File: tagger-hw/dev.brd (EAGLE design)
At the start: 65.7 x 62.2 mm, 51 parts, among them J2 22-23-2021, J3 22-23-2021, X1 EXC-31B

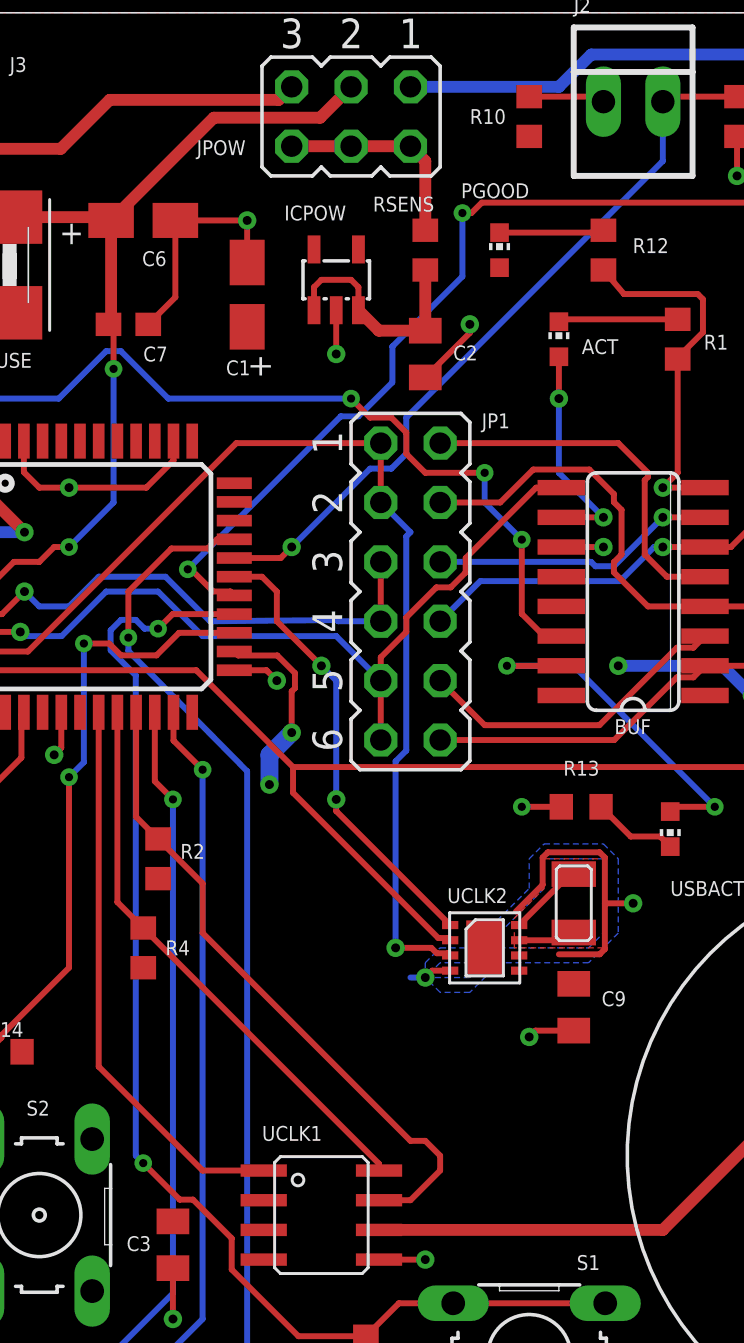
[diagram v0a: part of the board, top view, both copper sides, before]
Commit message: Add some test points
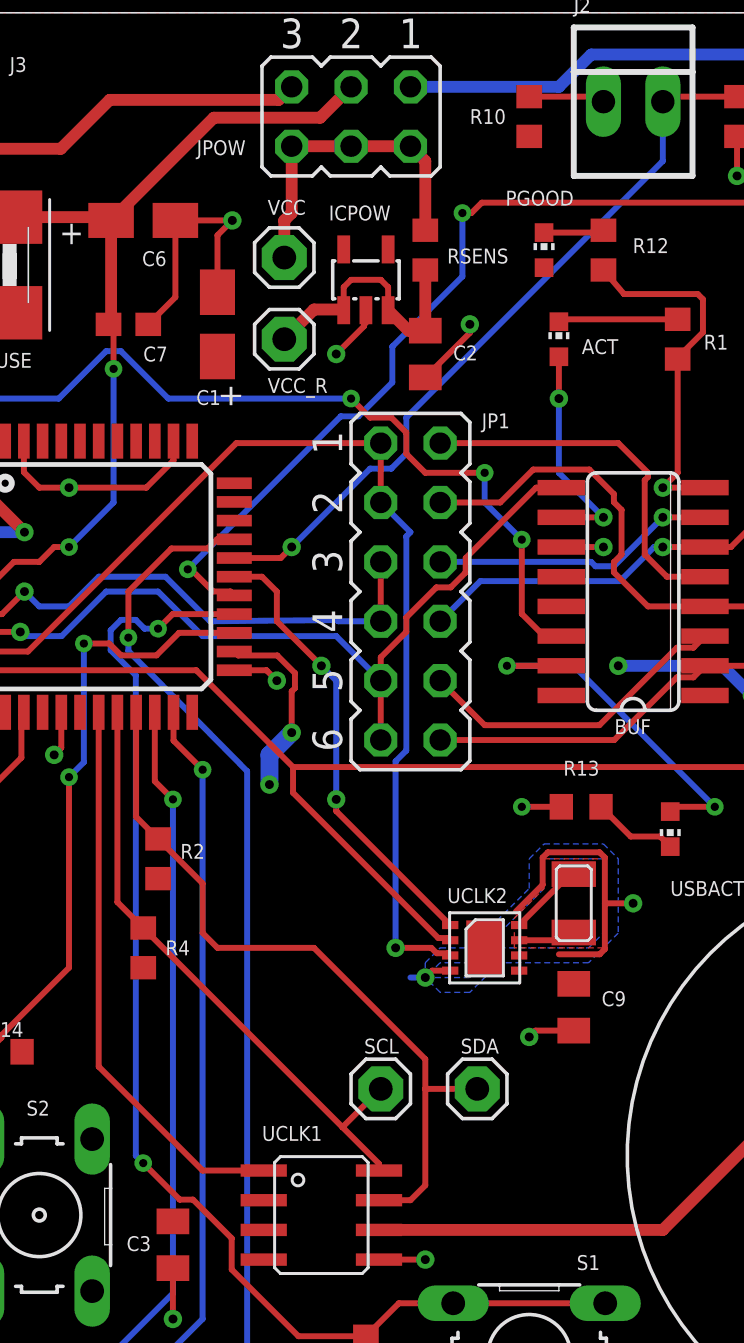
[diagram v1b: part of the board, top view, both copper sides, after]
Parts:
- added SCL, SDA, VCC, VCC_R: (no value), adafruit:1X01
- moved PGOOD 1.91 mm to (36.8, 52.1)
- moved C1 1.80 mm to (22.9, 48.9)
- moved ICPOW 1.27 mm to (29.2, 50.8)
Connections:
- net SCL: now also SCL.1
- net SDA: now also SDA.1
- net VCC: now also VCC.1
- net VCC_R: now also VCC_R.1
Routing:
- net VCC: track 8.94 -> 13.8 mm
- net SDA: track 28.5 -> 32.2 mm
- net SCL: track 24.2 -> 26.6 mm
- net +3V3_D: track 4.49 -> 2.58 mm
- net VCC_R: track 9.95 -> 11.7 mm
- net GND: track 127.6 -> 129.0 mm

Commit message: Switch to CR2032
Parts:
- removed BATT: CR2430H, battery:CR2430H
- added G1: CR2032H, battery:CR2032H
- C2, C3, C9: device adafruit:C0805K -> adafruit:C0603K
- renumbered J2 to JTRIG, J3 to JEXT
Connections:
- net GND: now also G1.-; no longer BATT.-
- net VBAT: now also G1.+; no longer BATT.+
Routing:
- net VBAT: track 102.8 -> 104.3 mm
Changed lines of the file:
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@@
 <attribute name="VALUE" x="20.535" y="50.845" size="0.635" layer="27" font="vector" rot="R270"/>
 </element>
-<element name="C2" library="adafruit" package="C0805K" value="0.1uF" x="31.75" y="47.625" smashed="yes" rot="R270">
+<element name="C2" library="adafruit" package="C0603K" value="0.1uF" x="31.75" y="47.625" smashed="yes" rot="R270">
 <attribute name="NAME" x="32.9425" y="47.355" size="0.635" layer="25" font="vector"/>
 <attribute name="VALUE" x="29.85" y="48.625" size="0.635" layer="27" font="vector" rot="R270"/>
@@
 <attribute name="VALUE" x="25.527" y="45.085" size="0.635" layer="27" font="vector" ratio="10" rot="R270"/>
 </element>
-<element name="C3" library="adafruit" package="C0805K" value="0.1uF" x="20.955" y="9.525" smashed="yes" rot="R270">
+<element name="C3" library="adafruit" package="C0603K" value="0.1uF" x="20.955" y="9.525" smashed="yes" rot="R270">
 <attribute name="NAME" x="18.9725" y="9.255" size="0.635" layer="25" font="vector"/>
 <attribute name="VALUE" x="19.055" y="10.525" size="0.635" layer="27" font="vector" rot="R270"/>
-</element>
-<element name="BATT" library="battery" library_urn="urn:adsk.eagle:library:109" package="CR2430H" package3d_urn="urn:adsk.eagle:package:4583/1" value="CR2430H" x="52.705" y="13.335" smashed="yes">
-<attribute name="NAME" x="49.403" y="26.67" size="0.635" layer="25" font="vector" ratio="10"/>
-<attribute name="VALUE" x="57.785" y="12.065" size="0.635" layer="27" font="vector" ratio="10" rot="R90"/>
 </element>
 <element name="JPOW" library="jumper" library_urn="urn:adsk.eagle:library:252" package="JP3Q" package3d_urn="urn:adsk.eagle:package:15460/1" value="HDR100IMP40M-G-V-TH" x="28.575" y="57.785" smashed="yes" rot="R180">
@@
 <attribute name="VALUE" x="32.69" y="19.9075" size="0.4" layer="27"/>
 </element>
-<element name="C9" library="adafruit" package="C0805K" value="0.1uF" x="38.1" y="19.685" smashed="yes" rot="R270">
+<element name="C9" library="adafruit" package="C0603K" value="0.1uF" x="38.1" y="19.685" smashed="yes" rot="R270">
 <attribute name="NAME" x="39.2925" y="19.7325" size="0.635" layer="25" font="vector"/>
 <attribute name="VALUE" x="36.2" y="20.685" size="0.635" layer="27" font="vector" rot="R270"/>
 </element>
 <element name="X1" library="dorskyee" package="XTAL-SM2" value="EXC-31B" x="38.1" y="24.13" smashed="yes" rot="R90"/>
-<element name="J2" library="con-molex" library_urn="urn:adsk.eagle:library:165" package="22-23-2021" value="22-23-2021" x="40.64" y="58.42" smashed="yes">
+<element name="JTRIG" library="con-molex" library_urn="urn:adsk.eagle:library:165" package="22-23-2021" value="22-23-2021" x="40.64" y="58.42" smashed="yes">
 <attribute name="MF" value="MOLEX" x="40.64" y="58.42" size="1.778" layer="27" display="off"/>
 <attribute name="MPN" value="22-23-2021" x="40.64" y="58.42" size="1.778" layer="27" display="off"/>
@@
 <attribute name="VALUE" x="46.99" y="57.15" size="0.635" layer="27" font="vector" rot="R90"/>
 </element>
-<element name="J3" library="con-molex" library_urn="urn:adsk.eagle:library:165" package="22-23-2021" value="22-23-2021" x="10.795" y="58.42" smashed="yes">
+<element name="JEXT" library="con-molex" library_urn="urn:adsk.eagle:library:165" package="22-23-2021" value="22-23-2021" x="10.795" y="58.42" smashed="yes">
 <attribute name="MF" value="MOLEX" x="10.795" y="58.42" size="1.778" layer="27" display="off"/>
 <attribute name="MPN" value="22-23-2021" x="10.795" y="58.42" size="1.778" layer="27" display="off"/>
@@
 <attribute name="VALUE" x="28.575" y="13.0175" size="1.27" layer="27"/>
 </element>
+<element name="G1" library="battery" library_urn="urn:adsk.eagle:library:109" package="CR2032H" package3d_urn="urn:adsk.eagle:package:4585/1" value="CR2032H" x="53.34" y="13.335"/>
 </elements>
 <signals>
@@
 <via x="31.75" y="8.89" extent="1-16" drill="0.381"/>
 <contactref element="C3" pad="2"/>
-<wire x1="20.955" y1="8.525" x2="20.955" y2="6.35" width="0.254" layer="1"/>
+<wire x1="20.955" y1="8.65" x2="20.955" y2="6.35" width="0.254" layer="1"/>
 <via x="20.955" y="6.35" extent="1-16" drill="0.381"/>
-<contactref element="BATT" pad="-"/>
 <contactref element="JUSB" pad="S6"/>
 <contactref element="JUSB" pad="S5"/>
@@
 <wire x1="45.085" y1="56.935" x2="45.085" y2="55.245" width="0.254" layer="1"/>
 <via x="45.085" y="55.245" extent="1-16" drill="0.381"/>
-<contactref element="J3" pad="2"/>
-<wire x1="36.195" y1="18.415" x2="36.465" y2="18.685" width="0.254" layer="1"/>
-<wire x1="36.465" y1="18.685" x2="38.1" y2="18.685" width="0.254" layer="1"/>
+<contactref element="JEXT" pad="2"/>
 <contactref element="L1" pad="1"/>
 <wire x1="1.27" y1="47.498" x2="1.905" y2="46.863" width="0.254" layer="1"/>
@@
 <wire x1="61.2675" y1="33.3275" x2="60.325" y2="32.385" width="0.254" layer="1"/>
 <via x="60.325" y="32.385" extent="1-16" drill="0.35"/>
-<wire x1="31.75" y1="46.625" x2="33.655" y2="48.53" width="0.254" layer="1"/>
-<wire x1="33.655" y1="48.53" x2="33.655" y2="48.895" width="0.254" layer="1"/>
 <wire x1="27.94" y1="47.625" x2="29.13" y2="48.815" width="0.254" layer="1"/>
 <wire x1="29.13" y1="48.815" x2="29.13" y2="48.88803125" width="0.254" layer="1"/>
@@
 <wire x1="22.86" y1="50.27" x2="22.86" y2="52.705" width="0.254" layer="1"/>
 <wire x1="22.86" y1="52.705" x2="23.495" y2="53.34" width="0.254" layer="1"/>
+<wire x1="38.1" y1="18.81" x2="37.705" y2="18.415" width="0.254" layer="1"/>
+<wire x1="37.705" y1="18.415" x2="36.195" y2="18.415" width="0.254" layer="1"/>
+<wire x1="31.75" y1="46.75" x2="33.655" y2="48.655" width="0.254" layer="1"/>
+<wire x1="33.655" y1="48.655" x2="33.655" y2="48.895" width="0.254" layer="1"/>
+<contactref element="G1" pad="-"/>
 </signal>
 <signal name="VCC">
@@
 <contactref element="JPOW" pad="1"/>
 <contactref element="UCLK1" pad="P$6"/>
-<contactref element="BATT" pad="+"/>
 <wire x1="37.46625625" y1="59.055" x2="31.115" y2="59.055" width="0.508" layer="16"/>
 <wire x1="37.46625625" y1="59.055" x2="38.84725625" y2="60.436" width="0.508" layer="16"/>
-<wire x1="29.77" y1="10.16" x2="41.91" y2="10.16" width="0.508" layer="1"/>
-<wire x1="41.91" y1="10.16" x2="57.785" y2="26.035" width="0.508" layer="1"/>
+<wire x1="29.77" y1="10.16" x2="44.45" y2="10.16" width="0.508" layer="1"/>
 <wire x1="60.5315" y1="60.436" x2="63.1825" y2="57.785" width="0.508" layer="16"/>
-<wire x1="63.1825" y1="44.1377" x2="63.7667" y2="43.5535" width="0.508" layer="16"/>
-<wire x1="63.7667" y1="43.5535" x2="63.7667" y2="32.0167" width="0.508" layer="16"/>
-<wire x1="63.7667" y1="32.0167" x2="57.785" y2="26.035" width="0.508" layer="16"/>
+<wire x1="63.7667" y1="43.5535" x2="63.1825" y2="44.1377" width="0.508" layer="16"/>
 <wire x1="63.1825" y1="57.785" x2="63.1825" y2="44.1377" width="0.508" layer="16"/>
 <wire x1="38.84725625" y1="60.436" x2="60.5315" y2="60.436" width="0.508" layer="16"/>
+<contactref element="G1" pad="+"/>
+<wire x1="58.42" y1="24.13" x2="44.45" y2="10.16" width="0.508" layer="1"/>
+<wire x1="58.42" y1="24.13" x2="63.7667" y2="29.4767" width="0.508" layer="16"/>
+<wire x1="63.7667" y1="29.4767" x2="63.7667" y2="43.5535" width="0.508" layer="16"/>
 </signal>
 <signal name="VBUS_F">
@@
 <signal name="VEXT">
 <contactref element="JPOW" pad="5"/>
-<contactref element="J3" pad="1"/>
+<contactref element="JEXT" pad="1"/>
 <wire x1="9.525" y1="58.42" x2="10.795" y2="57.15" width="0.508" layer="1"/>
 <wire x1="10.795" y1="57.15" x2="10.79625625" y2="57.15" width="0.508" layer="1"/>
@@
 </signal>
 <signal name="TRIG_L">
-<contactref element="J2" pad="2"/>
+<contactref element="JTRIG" pad="2"/>
 <contactref element="R11" pad="2"/>
 <contactref element="UC" pad="29"/>
@@
 </signal>
 <signal name="TRIG_H">
-<contactref element="J2" pad="1"/>
+<contactref element="JTRIG" pad="1"/>
 <contactref element="R10" pad="1"/>
 <wire x1="39.37" y1="58.42" x2="39.155" y2="58.635" width="0.254" layer="1"/>
@@
 <contactref element="RSENS" pad="1"/>
 <contactref element="C2" pad="1"/>
-<wire x1="31.75" y1="51.22" x2="31.75" y2="48.625" width="0.508" layer="1"/>
+<wire x1="31.75" y1="51.22" x2="31.75" y2="48.5" width="0.508" layer="1"/>
 <contactref element="VCC_R" pad="1"/>
 <wire x1="30.16" y1="49.5" x2="31.035" y2="48.625" width="0.508" layer="1"/>
-<wire x1="31.035" y1="48.625" x2="31.75" y2="48.625" width="0.508" layer="1"/>
+<wire x1="31.035" y1="48.625" x2="31.75" y2="48.5" width="0.508" layer="1"/>
 <wire x1="25.7175" y1="48.26" x2="26.9875" y2="49.53" width="0.508" layer="1"/>
 <wire x1="26.9875" y1="49.53" x2="28.26" y2="49.53" width="0.508" layer="1"/>
